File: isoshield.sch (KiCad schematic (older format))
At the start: 2 parts

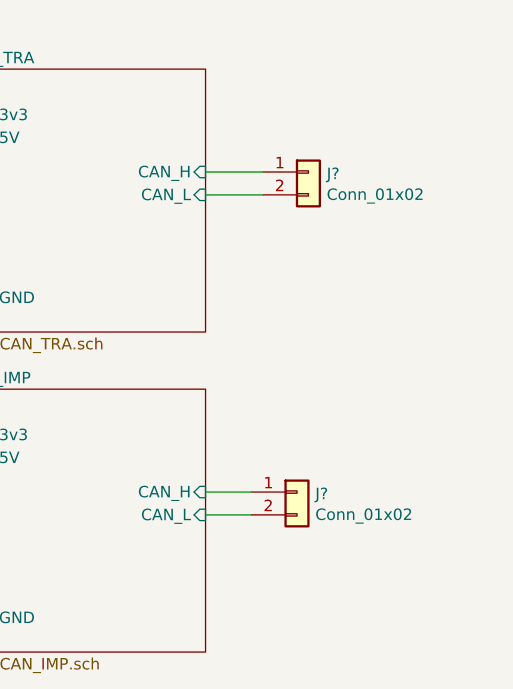
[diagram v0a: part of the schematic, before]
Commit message: Added labels to all components
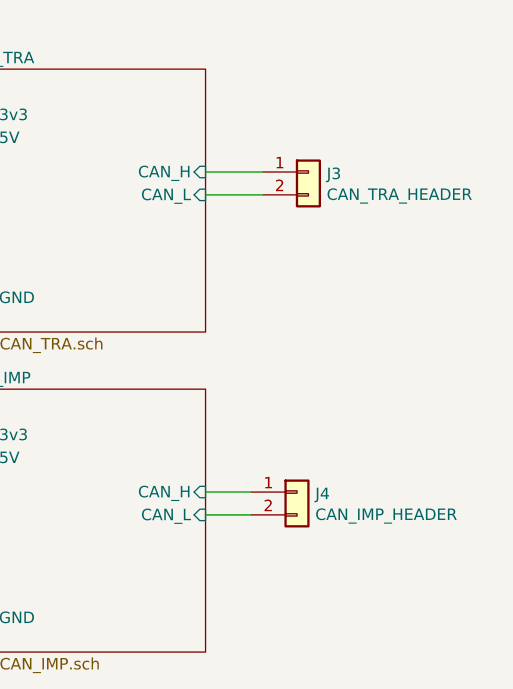
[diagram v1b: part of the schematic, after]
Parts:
- J3: renamed from J?; value Conn_01x02 -> CAN_TRA_HEADER
- J4: renamed from J?; value Conn_01x02 -> CAN_IMP_HEADER
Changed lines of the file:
@@
 encoding utf-8
 Sheet 1 7
-Title ""
+Title "AvenaShield for ISOBlue Avena"
 Date ""
-Rev ""
+Rev "1"
 Comp ""
 Comment1 ""
@@
 	6350 4450 6500 4450
 $Comp
-L Connector_Generic:Conn_01x02 J?
+L Connector_Generic:Conn_01x02 J3
 U 1 1 5E47DD56
 P 10000 4000
-F 0 "J?" H 10080 3992 50  0000 L CNN
-F 1 "Conn_01x02" H 10080 3901 50  0000 L CNN
+F 0 "J3" H 10080 3992 50  0000 L CNN
+F 1 "CAN_TRA_HEADER" H 10080 3901 50  0000 L CNN
 F 2 "TerminalBlock_Phoenix:TerminalBlock_Phoenix_PT-1,5-2-5.0-H_1x02_P5.00mm_Horizontal" H 10000 4000 50  0001 C CNN
 F 3 "~" H 10000 4000 50  0001 C CNN
@@
 $EndComp
 $Comp
-L Connector_Generic:Conn_01x02 J?
+L Connector_Generic:Conn_01x02 J4
 U 1 1 5E47E2F9
 P 9950 5400
-F 0 "J?" H 10030 5392 50  0000 L CNN
-F 1 "Conn_01x02" H 10030 5301 50  0000 L CNN
+F 0 "J4" H 10030 5392 50  0000 L CNN
+F 1 "CAN_IMP_HEADER" H 10030 5301 50  0000 L CNN
 F 2 "TerminalBlock_Phoenix:TerminalBlock_Phoenix_PT-1,5-2-5.0-H_1x02_P5.00mm_Horizontal" H 9950 5400 50  0001 C CNN
 F 3 "~" H 9950 5400 50  0001 C CNN
